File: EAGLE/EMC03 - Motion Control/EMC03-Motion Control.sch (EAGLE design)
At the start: 132 parts, among them J1 UART0, J10 S4B-PH-SM4, J11 S4B-PH-SM4, J12 S4B-PH-SM4, J13 S5B-PH-SM4, J14 S5B-PH-SM4, J15 S5B-PH-SM4, J17 S8B-PH-SM4, J19 S6B-PH-SM4, J2 FTSH-105-1-L-DV, J5 S3B-PH-SM4, J6 S3B-PH-SM4, J7 S3B-PH-SM4, Q1 12MHz, U1 LPC1768, U2 SP3485, U3 74LVC, U6 TMC2130-LA, U7 TMC2130-LA, U8 TMC2130-LA

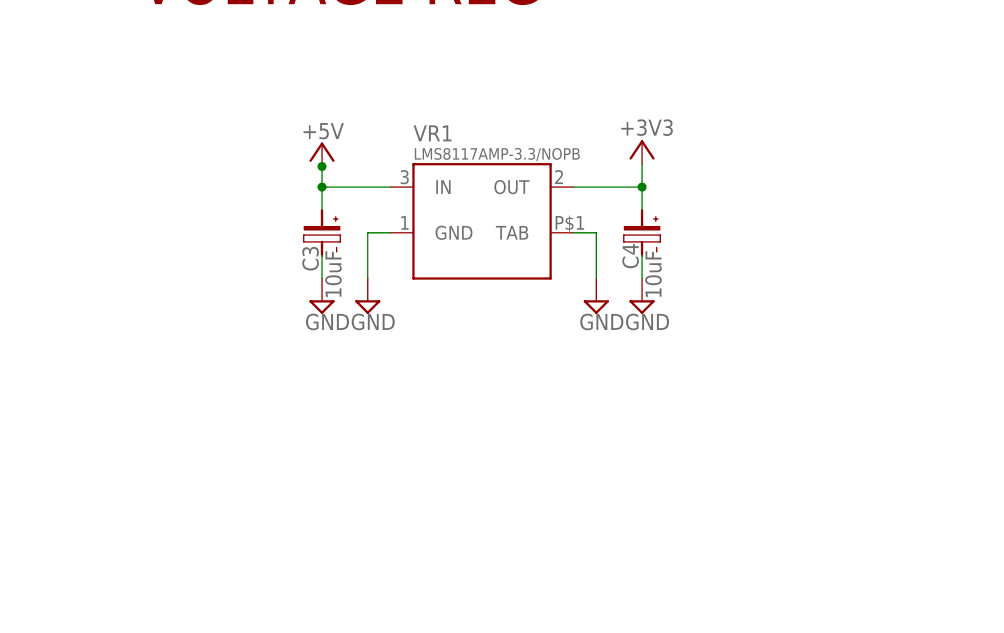
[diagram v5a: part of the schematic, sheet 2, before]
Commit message: Routing completed for EMC03, need to clean DRC, format. Routing completed for ECAM03.
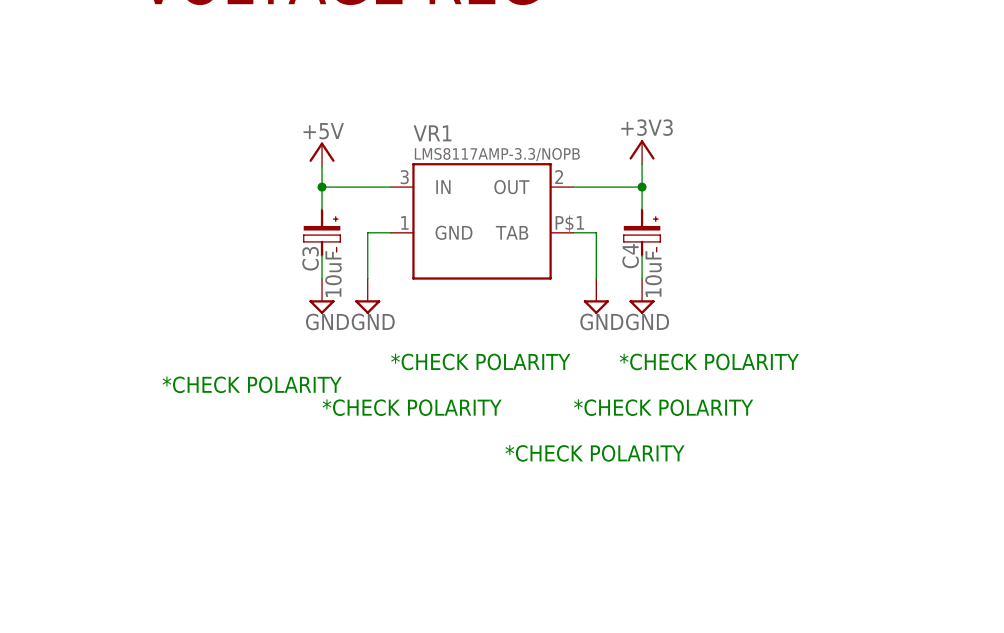
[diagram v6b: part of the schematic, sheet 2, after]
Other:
- note added: "*CHECK POLARITY"
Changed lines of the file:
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@@
 <text x="25.4" y="124.46" size="5.08" layer="94">OPTICAL ENCODERS</text>
 <text x="157.48" y="167.64" size="5.08" layer="94">VOLTAGE REG</text>
+<text x="185.42" y="127" size="1.778" layer="91">*CHECK POLARITY</text>
+<text x="177.8" y="121.92" size="1.778" layer="91">*CHECK POLARITY</text>
+<text x="198.12" y="116.84" size="1.778" layer="91">*CHECK POLARITY</text>
+<text x="205.74" y="121.92" size="1.778" layer="91">*CHECK POLARITY</text>
+<text x="160.02" y="124.46" size="1.778" layer="91">*CHECK POLARITY</text>
+<text x="210.82" y="127" size="1.778" layer="91">*CHECK POLARITY</text>
 </plain>
 <instances>
@@
 <junction x="177.8" y="147.32"/>
 <pinref part="P+10" gate="1" pin="+5V"/>
-<wire x1="177.8" y1="149.606" x2="177.8" y2="149.86" width="0.1524" layer="91"/>
-<junction x="177.8" y="149.606"/>
 </segment>
 </net>

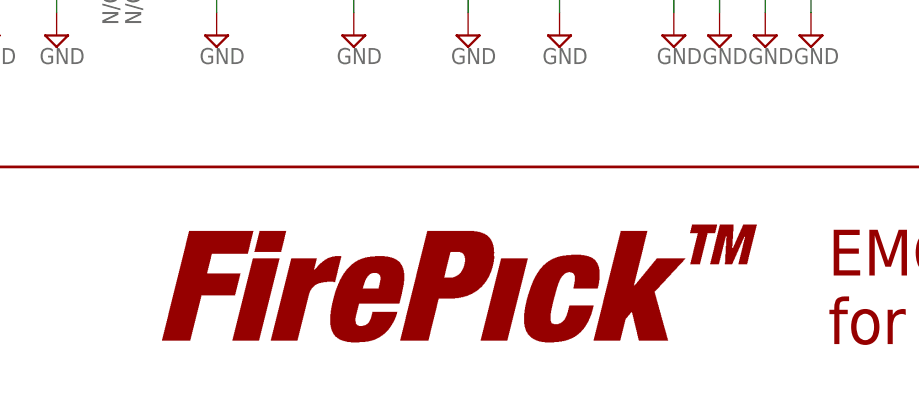
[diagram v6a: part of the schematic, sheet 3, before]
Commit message: Completed boards. Please look at airwires connecting thermal pads to GND vias. They shouldn't be present due to the vias.
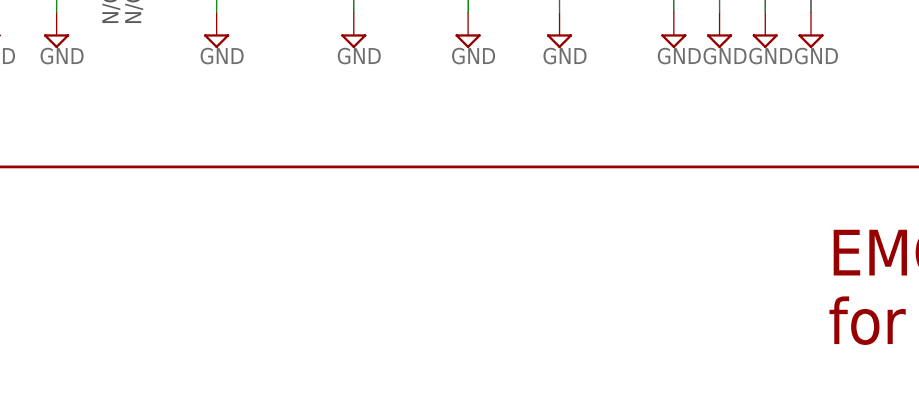
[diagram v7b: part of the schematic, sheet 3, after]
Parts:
- removed LOGO10: LOGO-FIREPICKLARGE, FirePick:LOGO-FIREPICKLARGE
- added TP2: +3.3V, TinWhiskers:TPAD
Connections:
- net +5V: now also TP2.2
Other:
- note added: "F PANEL"
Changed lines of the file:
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@@
 <attribute name="PARTNO" value="GRM188R71H223KA01D"/>
-</part>
-<part name="LOGO10" library="FirePick" deviceset="LOGO-FIREPICK" device="LARGE">
-<attribute name="BOM" value="EXCLUDE"/>
 </part>
 <part name="LOGO12" library="FirePick" deviceset="LOGO-FIREPICK" device="LARGE">
@@
 <part name="P+10" library="supply1" deviceset="+5V" device=""/>
 <part name="+3V2" library="supply1" deviceset="+3V3" device=""/>
+<part name="TP2" library="TinWhiskers" deviceset="TPAD" device="" value="+3.3V">
+<attribute name="DNP" value="T"/>
+<attribute name="PARTNO" value="N/A"/>
+</part>
+<part name="P+16" library="supply1" deviceset="+5V" device=""/>
 </parts>
 <sheets>
@@
 <text x="186.69" y="143.51" size="5.08" layer="94">RS-485 TRANSCEIVER</text>
 <text x="300.99" y="91.44" size="5.08" layer="94">SWD INTERFACE</text>
+<text x="350.52" y="137.16" size="5.08" layer="94">F PANEL</text>
 </plain>
 <instances>
@@
 <attribute name="VALUE" x="210.82" y="153.035" size="1.778" layer="96"/>
 </instance>
+<instance part="TP2" gate="G$1" x="292.1" y="223.52" rot="R90">
+<attribute name="DNP" x="292.1" y="223.52" size="1.778" layer="96" rot="R90" display="off"/>
+<attribute name="PARTNO" x="292.1" y="223.52" size="1.778" layer="96" display="off"/>
+</instance>
+<instance part="P+16" gate="1" x="292.1" y="233.426" smashed="yes">
+<attribute name="VALUE" x="289.814" y="233.934" size="1.778" layer="96"/>
+</instance>
 </instances>
 <busses>
@@
 <junction x="177.8" y="147.32"/>
 <pinref part="P+10" gate="1" pin="+5V"/>
+</segment>
+<segment>
+<pinref part="TP2" gate="G$1" pin="2"/>
+<wire x1="292.1" y1="226.06" x2="292.1" y2="230.886" width="0.1524" layer="91"/>
+<pinref part="P+16" gate="1" pin="+5V"/>
 </segment>
 </net>
@@
 <attribute name="PARTNO" x="96.52" y="220.98" size="1.778" layer="96" display="off"/>
 </instance>
-<instance part="LOGO10" gate="G$1" x="85.09" y="8.89">
-<attribute name="BOM" x="85.09" y="8.89" size="1.778" layer="96" display="off"/>
-</instance>
 <instance part="P+5" gate="1" x="144.78" y="243.84" smashed="yes">

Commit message: Updated all boards to include changes for production
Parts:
- C11, C12, C13, C14, C18, C19, C20, C21, C22, C3, C4, R10, R11, R12, TB1, U3, VR1: PARTNO (none) -> *
- S1: value SWS001 -> CPL-SW-MOM-147873-2; device smd-special:SWS001 -> TinWhiskers:CPL-SW-MOM-147873-2
- S2, S3: device TinWhiskers:CPL-SW-MOM-0603 -> TinWhiskers:CPL-SW-MOM-147873-2
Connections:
- net +3V3: now also VR1.TAB; no longer VR1.OUT
- net GND: no longer VR1.TAB
